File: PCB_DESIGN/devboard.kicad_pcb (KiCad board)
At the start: 2 copper layers, 21 x 51 mm, 33 parts, among them J1 USB_C_Receptacle_USB2.0_14P, J2 Conn_01x20, J3 Conn_01x20, J4 Conn_01x03, SW1 SW_Push, U1 RP2040, U2 MCP1700x-330xxTT, U4 W25Q16JVUXIQ TR, Y1 12 MHz

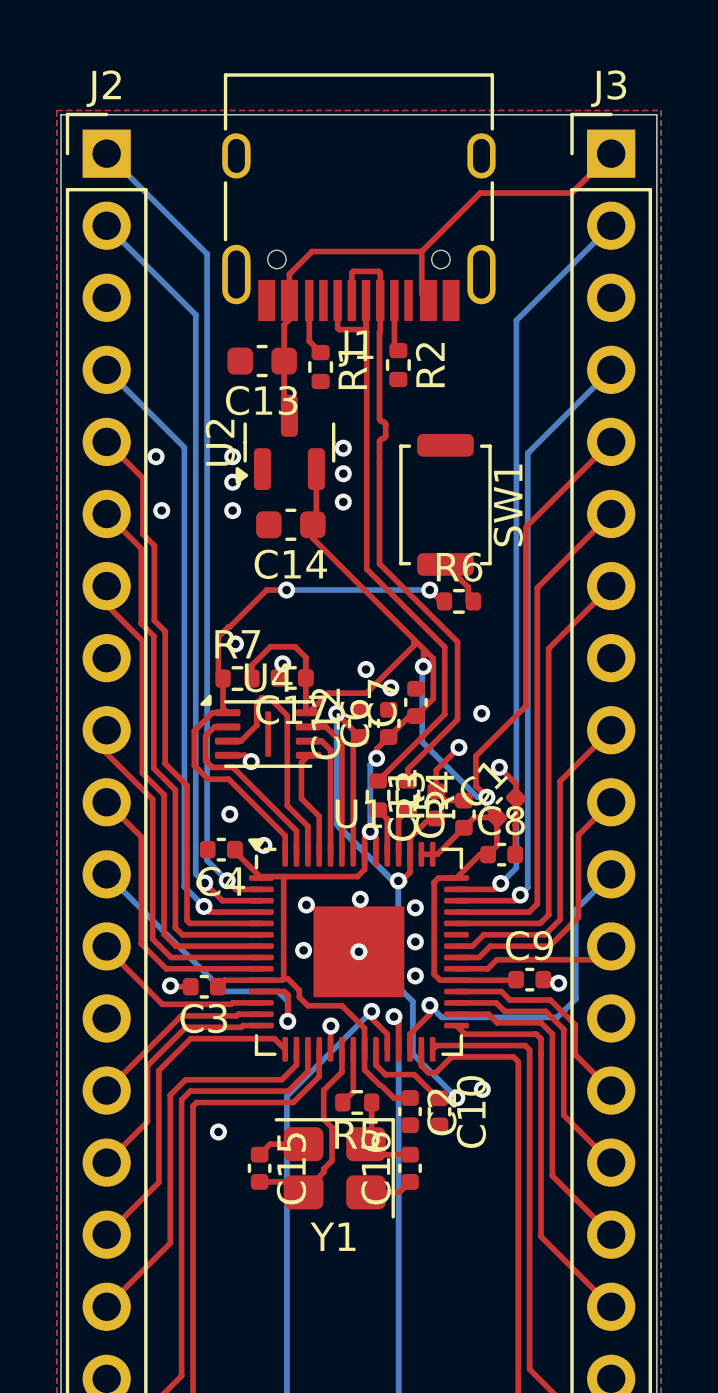
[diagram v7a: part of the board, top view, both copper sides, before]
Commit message: fixed all thermal relief errors
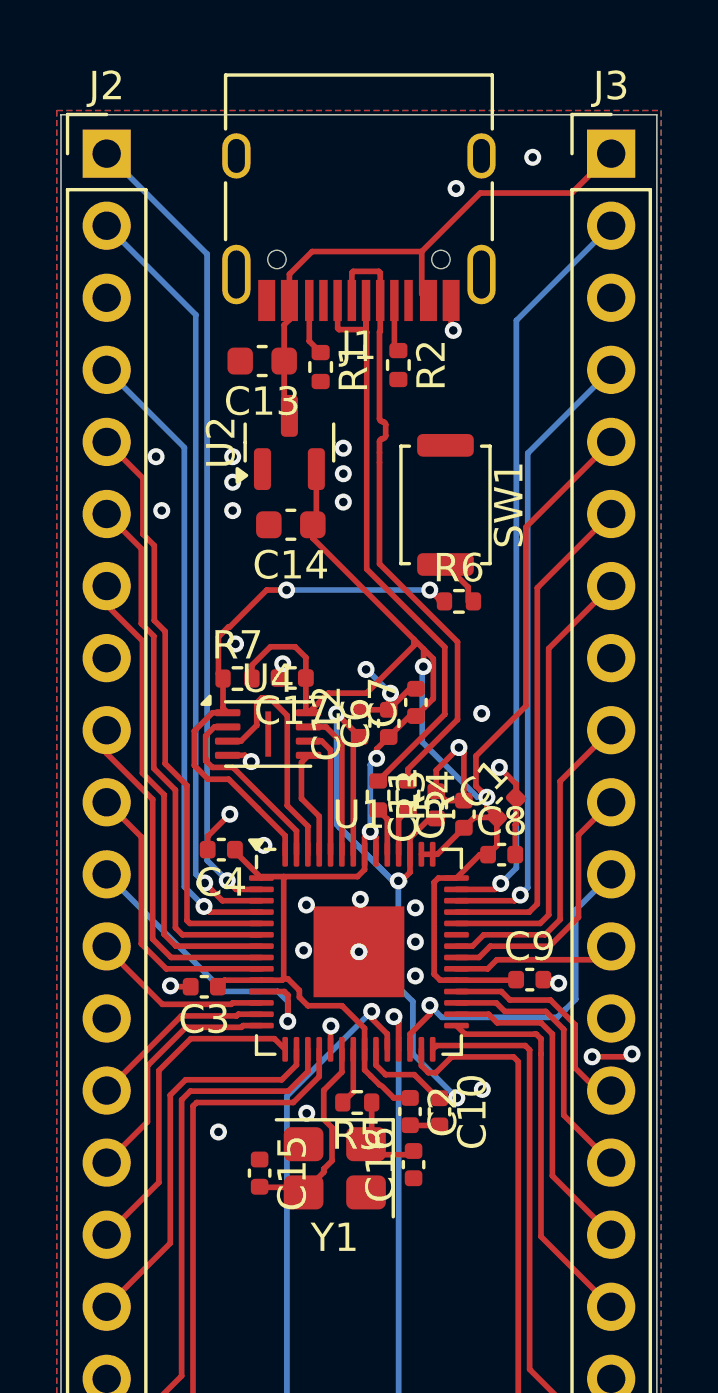
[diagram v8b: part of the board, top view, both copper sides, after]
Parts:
- moved C16 0.18 mm to (155.3, 119.1)
- moved C15 0.17 mm to (149.9, 119.4)
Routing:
- net GND: track 13.3 -> 22.0 mm, vias 30 -> 36
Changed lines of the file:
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@@
 	(footprint "Capacitor_SMD:C_0402_1005Metric"
 		(layer "F.Cu")
-		(at 149.875 119.23 -90)
+		(at 149.875 119.4 -90)
 		(descr "Capacitor SMD 0402 (1005 Metric), square (rectangular) end terminal, IPC-7351 nominal, (Body size source: IPC-SM-782 page 76, https://www.pcb-3d.com/wordpress/wp-content/uploads/ipc-sm-782a_amendment_1_and_2.pdf), generated with kicad-footprint-generator")
 		(tags "capacitor")
@@
 	(footprint "Capacitor_SMD:C_0402_1005Metric"
 		(layer "F.Cu")
-		(at 155.175 119.23 90)
+		(at 155.3 119.1 90)
 		(descr "Capacitor SMD 0402 (1005 Metric), square (rectangular) end terminal, IPC-7351 nominal, (Body size source: IPC-SM-782 page 76, https://www.pcb-3d.com/wordpress/wp-content/uploads/ipc-sm-782a_amendment_1_and_2.pdf), generated with kicad-footprint-generator")
 		(tags "capacitor")
@@
 	)
 	(segment
+		(start 154.425 102.548472)
+		(end 154.486736 102.486736)
+		(width 0.2)
+		(layer "F.Cu")
+		(net 1)
+	)
+	(segment
 		(start 158.885 107.115)
 		(end 158.885 108.175)
@@
 	)
 	(segment
+		(start 162.9 115.3)
+		(end 163 115.2)
+		(width 0.2)
+		(layer "F.Cu")
+		(net 1)
+	)
+	(segment
 		(start 156.1 105.2)
 		(end 156.9 104.4)
@@
 	)
 	(segment
-		(start 154.805 120.08)
-		(end 155.175 119.71)
+		(start 156.625 88.645)
+		(end 156.625 89.625)
 		(width 0.2)
 		(layer "F.Cu")
@@
 	)
 	(segment
+		(start 154.425 103.07)
+		(end 154.425 102.548472)
+		(width 0.2)
+		(layer "F.Cu")
+		(net 1)
+	)
+	(segment
+		(start 148.045 107.53)
+		(end 148.825 106.75)
+		(width 0.2)
+		(layer "F.Cu")
+		(net 1)
+	)
+	(segment
 		(start 152.375 114.227581)
 		(end 152.375 115.0375)
@@
 	)
 	(segment
+		(start 155.185 117.72)
+		(end 155.175 117.71)
+		(width 0.2)
+		(layer "F.Cu")
+		(net 1)
+	)
+	(segment
+		(start 155.385 102.33)
+		(end 155.165 102.33)
+		(width 0.2)
+		(layer "F.Cu")
+		(net 1)
+	)
+	(segment
 		(start 159.875 112.58)
 		(end 160.288559 112.58)
@@
 	)
 	(segment
-		(start 150.245 118.38)
-		(end 149.875 118.75)
+		(start 148.045 108)
+		(end 148.045 107.53)
 		(width 0.2)
 		(layer "F.Cu")
@@
 	)
 	(segment
-		(start 153.625 120.08)
-		(end 154.805 120.08)
+		(start 157.075 104.575)
+		(end 156.9 104.4)
+		(width 0.2)
+		(layer "F.Cu")
+		(net 1)
+	)
+	(segment
+		(start 156.215 117.72)
+		(end 155.185 117.72)
+		(width 0.2)
+		(layer "F.Cu")
+		(net 1)
+	)
+	(segment
+		(start 155.165 102.33)
+		(end 154.425 103.07)
 		(width 0.2)
 		(layer "F.Cu")
@@
 	)
 	(segment
+		(start 154.425 103.07)
+		(end 153.405 103.07)
+		(width 0.2)
+		(layer "F.Cu")
+		(net 1)
+	)
+	(segment
 		(start 152.387649 114.214932)
 		(end 152.375 114.227581)
@@
 	)
 	(segment
+		(start 151.425 117.398527)
+		(end 151.535 117.288527)
+		(width 0.2)
+		(layer "F.Cu")
+		(net 1)
+	)
+	(segment
 		(start 160.288559 112.58)
 		(end 160.415 112.706441)
@@
 	)
 	(segment
-		(start 151.425 118.38)
-		(end 150.245 118.38)
+		(start 158.914411 106.185589)
+		(end 158.914411 105.689411)
 		(width 0.2)
 		(layer "F.Cu")
@@
 	)
 	(segment
-		(start 158.914411 106.185589)
-		(end 158.914411 105.689411)
+		(start 153.405 103.07)
+		(end 153.4 103.065)
 		(width 0.2)
 		(layer "F.Cu")
@@
 	)
 	(segment
+		(start 162.265 113.95)
+		(end 162.265 114.63)
+		(width 0.2)
+		(layer "F.Cu")
+		(net 1)
+	)
+	(segment
+		(start 157.075 106.27)
+		(end 157.075 104.575)
+		(width 0.2)
+		(layer "F.Cu")
+		(net 1)
+	)
+	(segment
+		(start 161.595 115.3)
+		(end 162.9 115.3)
+		(width 0.2)
+		(layer "F.Cu")
+		(net 1)
+	)
+	(segment
 		(start 147.445 112.83)
 		(end 146.763008 112.83)
@@
 		(net 1)
 	)
+	(segment
+		(start 156.625 89.625)
+		(end 156.7 89.7)
+		(width 0.2)
+		(layer "F.Cu")
+		(net 1)
+	)
+	(via
+		(at 156.8 84.7)
+		(size 0.6)
+		(drill 0.3)
+		(layers "F.Cu" "B.Cu")
+		(free yes)
+		(net 1)
+	)
 	(via
 		(at 146.225 94.15)
@@
 	)
 	(via
-		(at 158.325 105.1)
+		(at 151.535 117.288527)
 		(size 0.6)
 		(drill 0.3)
@@
 	)
 	(via
-		(at 150.025 107.85)
+		(at 158.325 105.1)
 		(size 0.6)
 		(drill 0.3)
 		(layers "F.Cu" "B.Cu")
-		(free yes)
 		(net 1)
 	)
 	(via
-		(at 154.5 102.3)
+		(at 150.025 107.85)
 		(size 0.6)
 		(drill 0.3)
@@
 	)
 	(via
+		(at 156.7 89.7)
+		(size 0.6)
+		(drill 0.3)
+		(layers "F.Cu" "B.Cu")
+		(net 1)
+	)
+	(via
 		(at 148.425 117.95)
 		(size 0.6)
@@
 	)
 	(via
+		(at 159.5 83.6)
+		(size 0.6)
+		(drill 0.3)
+		(layers "F.Cu" "B.Cu")
+		(free yes)
+		(net 1)
+	)
+	(via
 		(at 150.690446 101.45)
 		(size 0.6)
@@
 	)
 	(via
+		(at 154.486736 102.486736)
+		(size 0.6)
+		(drill 0.3)
+		(layers "F.Cu" "B.Cu")
+		(net 1)
+	)
+	(via
 		(at 148.925 94.15)
 		(size 0.6)
@@
 	)
 	(via
+		(at 163 115.2)
+		(size 0.6)
+		(drill 0.3)
+		(layers "F.Cu" "B.Cu")
+		(net 1)
+	)
+	(via
 		(at 146.733008 112.8)
 		(size 0.6)
@@
 	)
 	(via
+		(at 161.595 115.3)
+		(size 0.6)
+		(drill 0.3)
+		(layers "F.Cu" "B.Cu")
+		(net 1)
+	)
+	(via
 		(at 149.579265 104.895735)
 		(size 0.6)
@@
 	)
 	(segment
+		(start 153.625 101.65)
+		(end 153.65 101.65)
+		(width 0.2)
+		(layer "B.Cu")
+		(net 1)
+	)
+	(segment
+		(start 153.65 101.65)
+		(end 154.486736 102.486736)
+		(width 0.2)
+		(layer "B.Cu")
+		(net 1)
+	)
+	(segment
 		(start 151.276 112.959242)
 		(end 150.866758 112.55)
@@
 	)
 	(segment
-		(start 151.055 119.71)
-		(end 151.425 120.08)
-		(width 0.2)
-		(layer "F.Cu")
-		(net 5)
-	)
-	(segment
 		(start 152.426 117.79484)
 		(end 152.426 118.96516)
@@
 	)
 	(segment
-		(start 149.875 119.71)
-		(end 151.055 119.71)
+		(start 150.065 119.9)
+		(end 151.245 119.9)
 		(width 0.2)
 		(layer "F.Cu")
@@
 	)
 	(segment
+		(start 149.875 119.71)
+		(end 150.065 119.9)
+		(width 0.2)
+		(layer "F.Cu")
+		(net 5)
+	)
+	(segment
+		(start 151.245 119.9)
+		(end 151.425 120.08)
+		(width 0.2)
+		(layer "F.Cu")
+		(net 5)
+	)
+	(segment
 		(start 152.775 115.84)
 		(end 152.135 116.48)
@@
 	)
 	(segment
+		(start 158.39745 113)
+		(end 158.69745 113.3)
+		(width 0.2)
+		(layer "F.Cu")
+		(net 32)
+	)
+	(segment
 		(start 156.8125 113)
 		(end 158.39745 113)
@@
 	)
 	(segment
-		(start 160.995 114.17)
-		(end 160.995 115.22)
+		(start 160.125 113.3)
+		(end 160.995 114.17)
 		(width 0.2)
 		(layer "F.Cu")
@@
 	)
 	(segment
-		(start 158.39745 113)
-		(end 158.69745 113.3)
+		(start 158.69745 113.3)
+		(end 160.125 113.3)
 		(width 0.2)
 		(layer "F.Cu")
@@
 	)
 	(segment
-		(start 160.125 113.3)
-		(end 160.995 114.17)
+		(start 160.995 115.695)
+		(end 161.79 116.49)
 		(width 0.2)
 		(layer "F.Cu")
@@
 	)
 	(segment
-		(start 158.69745 113.3)
-		(end 160.125 113.3)
+		(start 160.995 114.17)
+		(end 160.995 115.695)
 		(width 0.2)
 		(layer "F.Cu")
@@
 	)
 	(segment
-		(start 160.995 115.22)
+		(start 161.79 116.49)
 		(end 162.265 116.49)
 		(width 0.2)
